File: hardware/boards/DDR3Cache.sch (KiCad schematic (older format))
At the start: 3 parts, among them U1 ECP5UM5G-381caBGA, U4 IS43TR16256B-125KBL

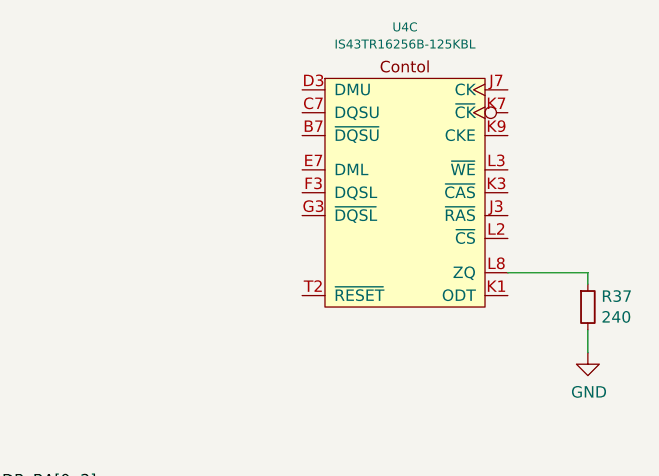
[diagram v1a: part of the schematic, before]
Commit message: Some ERC cleanup
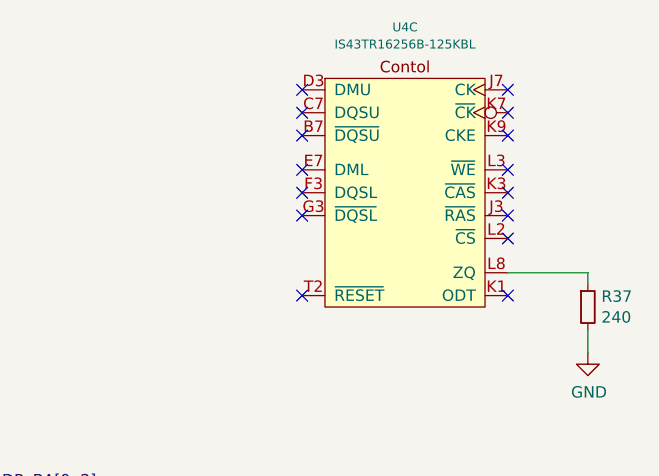
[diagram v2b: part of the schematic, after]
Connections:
- no-connect marks 65 -> 80
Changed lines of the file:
@@
 Wire Wire Line
 	13200 2350 12850 2350
+NoConn ~ 11950 1550
+NoConn ~ 11950 1650
+NoConn ~ 11950 1750
+NoConn ~ 11950 1900
+NoConn ~ 11950 2000
+NoConn ~ 11950 2100
+NoConn ~ 11950 2450
+NoConn ~ 12850 2450
+NoConn ~ 12850 2200
+NoConn ~ 12850 2100
+NoConn ~ 12850 2000
+NoConn ~ 12850 1900
+NoConn ~ 12850 1750
+NoConn ~ 12850 1650
+NoConn ~ 12850 1550
 Wire Bus Line
-	10550 3100 10550 3300
+	9250 4000 9250 4700
 Wire Bus Line
 	9250 3100 9250 3800
 Wire Bus Line
-	9250 4000 9250 4700
+	10550 3500 10550 5000
 Wire Bus Line
-	10550 3500 10550 5000
+	10550 3100 10550 3300
 $EndSCHEMATC

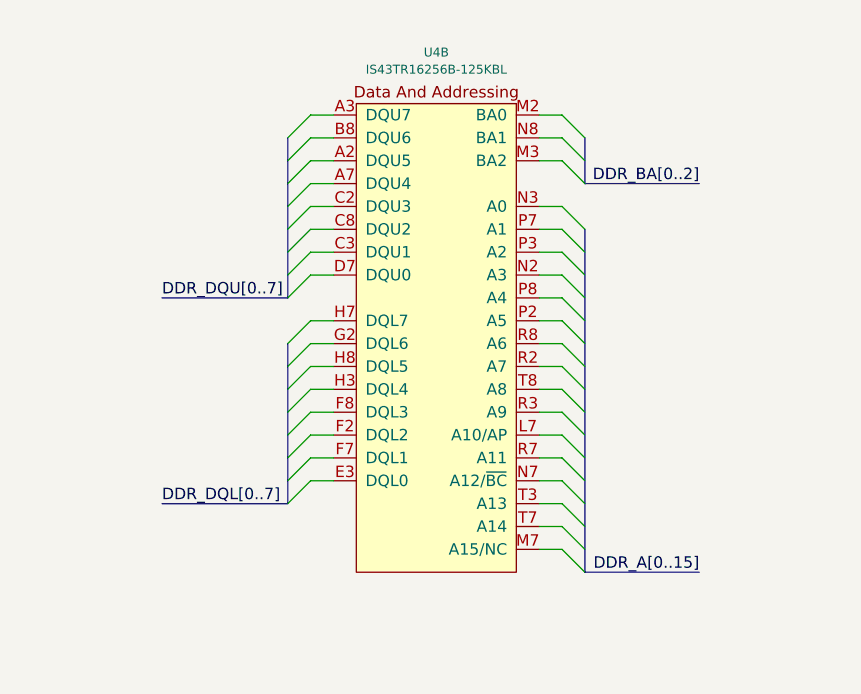
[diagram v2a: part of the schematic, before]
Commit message: Added headers for the SPI flash for both the FPGA and the PHY
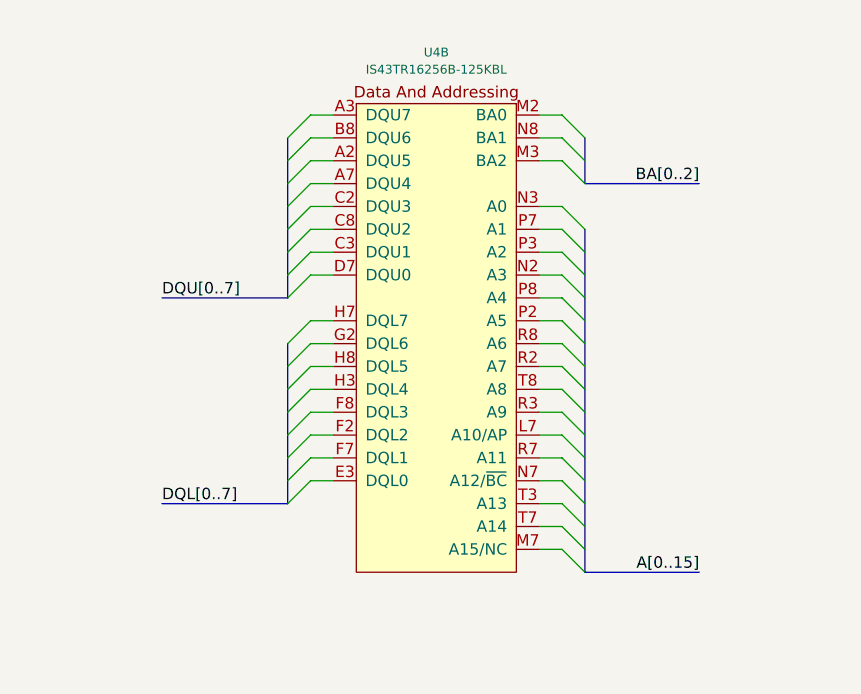
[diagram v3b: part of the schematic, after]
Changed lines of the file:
@@
 $Descr A3 16535 11693
 encoding utf-8
-Sheet 10 11
+Sheet 9 11
 Title "lethallink"
 Date "2020-06-13"
@@
 	9250 3800 8700 3800
 Text Label 11050 3300 2    50   ~ 0
-DDR_BA[0..2]
+BA[0..2]
 Text Label 11050 5000 2    50   ~ 0
-DDR_A[0..15]
+A[0..15]
 Text Label 8700 4700 0    50   ~ 0
-DDR_DQL[0..7]
+DQL[0..7]
 Text Label 8700 3800 0    50   ~ 0
-DDR_DQU[0..7]
+DQU[0..7]
 $Comp
 L Device:R_Small R37

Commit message: Some strugglebusting with the DDR interface
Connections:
- net BA2: now reaches U1.M3 (PL62B)
- net BA2: now also U4.M3 (BA2)
- net BA1: now reaches U1.N3 (PL62A)
- net BA1: now also U4.N8 (BA1)
- net A0: now reaches U1.P3 (PL68C/LLC/GPLL0T_IN)
- net A0: now also U4.N3 (A0)
- net BA0: now reaches U1.P5 (PL59D)
- net BA0: now also U4.M2 (BA0)
- net A14: now reaches U1.A3 (PL14C)
- net A14: now also U4.T7 (A14)
- net A4: now reaches U1.B3 (PL14D)
- net A4: now also U1.D2 (PL26C), U4.P8 (A4)
- net A11: now reaches U1.B4 (PL14B)
- net A11: now also U4.R7 (A11)
- net A6: now reaches U1.B5 (PL11C)
- net A6: now also U4.R8 (A6)
- net A12: now reaches U1.C3 (PL17C)
- net A12: now also U4.N7 (A12/~BC)
- net A1: now reaches U1.C4 (PL14A)
- net A1: now also U4.P7 (A1)
- net A8: now reaches U1.C5 (PL11D)
- net A8: now also U4.T8 (A8)
- net A13: now reaches U1.D3 (PL17D)
- net A13: now also U4.T3 (A13)
- net A10: now reaches U1.D5 (PL17B)
- net A10: now also U4.L7 (A10/AP)
- net A9: now reaches U1.E3 (PL20B)
- net A9: now also U4.R3 (A9)
- net A7: now reaches U1.E4 (PL17A)
- net A7: now also U4.R2 (A7)
- net A2: now reaches U1.E5 (PL20C)
- net A2: now also U4.P3 (A2)
- net A5: now reaches U1.F4 (PL20A)
- net A5: now also U4.P2 (A5)
- net A3: now reaches U1.F5 (PL20D)
- net A3: now also U4.N2 (A3)
- net DQU5: now reaches U4.A2 (DQU5)
- net DQU7: now reaches U4.A3 (DQU7)
- net DQU4: now reaches U4.A7 (DQU4)
- net DQU6: now reaches U4.B8 (DQU6)
- net DQU3: now reaches U4.C2 (DQU3)
- net DQU1: now reaches U4.C3 (DQU1)
- net DQU2: now reaches U4.C8 (DQU2)
- net DQU0: now reaches U4.D7 (DQU0)
- net DQL0: now reaches U4.E3 (DQL0)
- net DQL2: now reaches U4.F2 (DQL2)
- net DQL1: now reaches U4.F7 (DQL1)
- net DQL3: now reaches U4.F8 (DQL3)
- net DQL6: now reaches U4.G2 (DQL6)
- net DQL4: now reaches U4.H3 (DQL4)
- net DQL7: now reaches U4.H7 (DQL7)
- net DQL5: now reaches U4.H8 (DQL5)
- net A15: now reaches U4.M7 (A15/NC)
- no-connect marks 80 -> 61

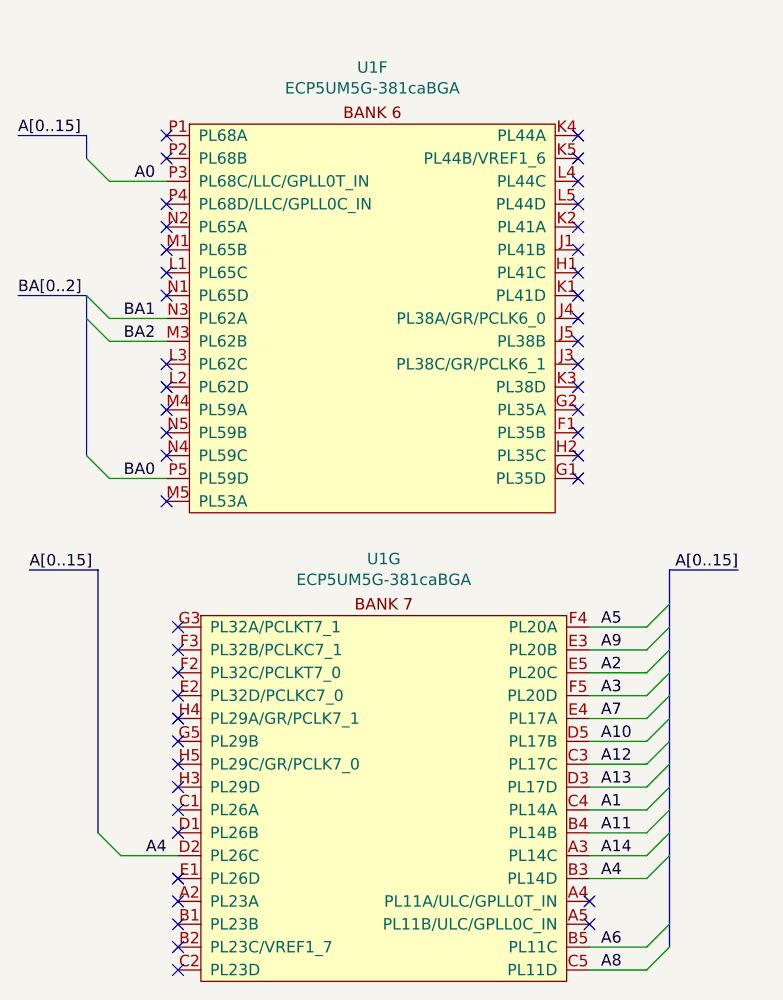
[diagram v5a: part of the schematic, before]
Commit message: Moved some things around swapping the DDR from banks 7 and 8 to banks 2 and 3, and moved the GPIFF 2 stuff to bank 7 to stop them from crossing over
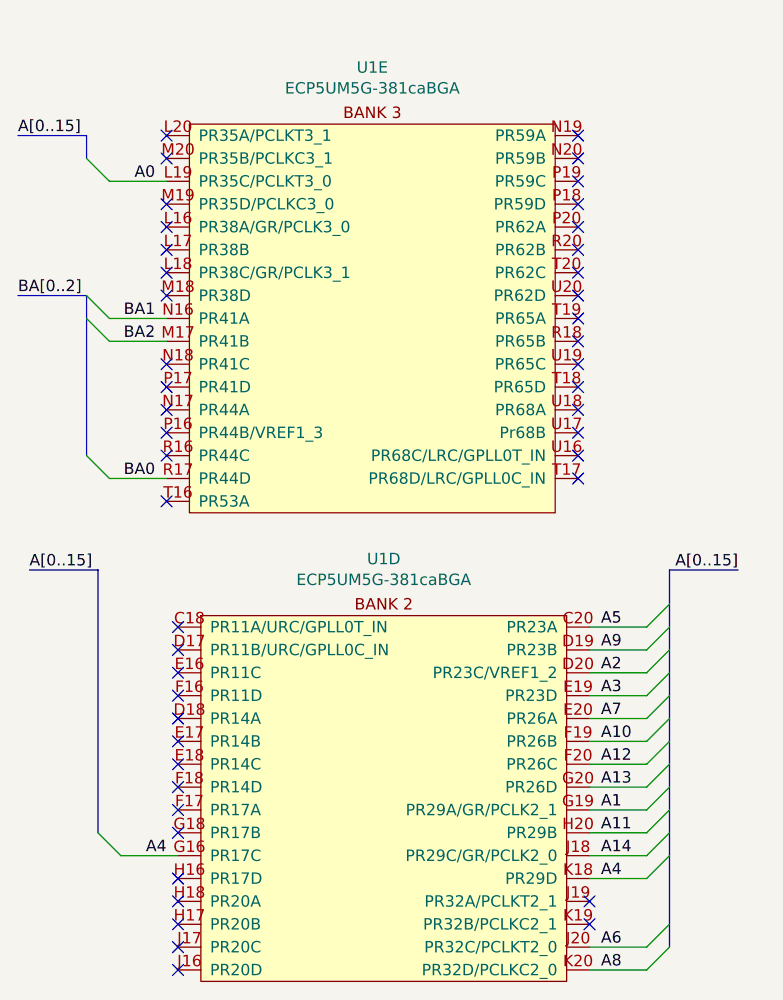
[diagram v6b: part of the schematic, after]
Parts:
- removed U1: ECP5UM5G-381caBGA, lethalbit:318caBGA, symbol lethalbit:ECP5UM5G-381caBGA
- added U1: ECP5UM5G-381caBGA, lethalbit:318caBGA, symbol lethalbit:ECP5UM5G-381caBGA
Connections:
- net A0: now also U1.L19 (PR35C/PCLKT3_0)
- net A1: now also U1.G19 (PR29A/GR/PCLK2_1)
- net A10: now also U1.F19 (PR26B)
- net A11: now also U1.H20 (PR29B)
- net A12: now also U1.F20 (PR26C)
- net A13: now also U1.G20 (PR26D)
- net A14: now also U1.J18 (PR29C/GR/PCLK2_0)
- net A2: now also U1.D20 (PR23C/VREF1_2)
- net A3: now also U1.E19 (PR23D)
- net A4: now also U1.G16 (PR17C), U1.K18 (PR29D)
- net A5: now also U1.C20 (PR23A)
- net A6: now also U1.J20 (PR32C/PCLKT2_0)
- net A7: now also U1.E20 (PR26A)
- net A8: now also U1.K20 (PR32D/PCLKC2_0)
- net A9: now also U1.D19 (PR23B)
- net BA0: now also U1.R17 (PR44D)
- net BA1: now also U1.N16 (PR41A)
- net BA2: now also U1.M17 (PR41B)
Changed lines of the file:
@@
 Comment4 ""
 $EndDescr
-$Comp
-L lethalbit:ECP5UM5G-381caBGA U1
-U 6 1 5F1BFFB3
-P 5850 1800
-F 0 "U1" H 5850 2148 50  0000 C CNN
-F 1 "ECP5UM5G-381caBGA" H 5850 2057 50  0000 C CNN
-F 2 "lethalbit:318caBGA" H 4500 1950 50  0001 C CNN
-F 3 "" H 4500 1950 50  0001 C CNN
-F 4 "Lattice" H 5850 1800 50  0001 C CNN "MFR"
-F 5 "LFE5UM5G-85F-8BG381I" H 5850 1800 50  0001 C CNN "MPN"
-F 6 "220-2112-ND" H 5850 1800 50  0001 C CNN "DIGIKEY_PN"
-	6    5850 1800
-	1    0    0    -1
-$EndComp
-$Comp
-L lethalbit:ECP5UM5G-381caBGA U1
-U 7 1 5F1BFFB9
-P 5900 3950
-F 0 "U1" H 5900 4298 50  0000 C CNN
-F 1 "ECP5UM5G-381caBGA" H 5900 4207 50  0000 C CNN
-F 2 "lethalbit:318caBGA" H 4550 4100 50  0001 C CNN
-F 3 "" H 4550 4100 50  0001 C CNN
-F 4 "Lattice" H 5900 3950 50  0001 C CNN "MFR"
-F 5 "LFE5UM5G-85F-8BG381I" H 5900 3950 50  0001 C CNN "MPN"
-F 6 "220-2112-ND" H 5900 3950 50  0001 C CNN "DIGIKEY_PN"
-	7    5900 3950
-	1    0    0    -1
-$EndComp
 NoConn ~ 4950 1750
 NoConn ~ 4950 1850
@@
 Wire Bus Line
 	4650 3650 4650 4800
+$Comp
+L lethalbit:ECP5UM5G-381caBGA U?
+U 4 1 5FCBABF4
+P 5900 3950
+AR Path="/5EF6A128/5FCBABF4" Ref="U?"  Part="4"
+AR Path="/5F2CAFD2/5FCBABF4" Ref="U?"  Part="4"
+AR Path="/5EDF3898/5FCBABF4" Ref="U1"  Part="4"
+F 0 "U1" H 5900 4298 50  0000 C CNN
+F 1 "ECP5UM5G-381caBGA" H 5900 4207 50  0000 C CNN
+F 2 "lethalbit:318caBGA" H 4550 4100 50  0001 C CNN
+F 3 "" H 4550 4100 50  0001 C CNN
+F 4 "Lattice" H 5900 3950 50  0001 C CNN "MFR"
+F 5 "LFE5UM5G-85F-8BG381I" H 5900 3950 50  0001 C CNN "MPN"
+F 6 "220-2112-ND" H 5900 3950 50  0001 C CNN "DIGIKEY_PN"
+	4    5900 3950
+	1    0    0    -1
+$EndComp
+$Comp
+L lethalbit:ECP5UM5G-381caBGA U?
+U 5 1 5FCF1F26
+P 5850 1800
+AR Path="/5EF67D90/5FCF1F26" Ref="U?"  Part="5"
+AR Path="/5F2CAFD2/5FCF1F26" Ref="U?"  Part="5"
+AR Path="/5EF6A128/5FCF1F26" Ref="U?"  Part="5"
+AR Path="/5EDF3898/5FCF1F26" Ref="U1"  Part="5"
+F 0 "U1" H 5850 2148 50  0000 C CNN
+F 1 "ECP5UM5G-381caBGA" H 5850 2057 50  0000 C CNN
+F 2 "lethalbit:318caBGA" H 4500 1950 50  0001 C CNN
+F 3 "" H 4500 1950 50  0001 C CNN
+F 4 "Lattice" H 5850 1800 50  0001 C CNN "MFR"
+F 5 "LFE5UM5G-85F-8BG381I" H 5850 1800 50  0001 C CNN "MPN"
+F 6 "220-2112-ND" H 5850 1800 50  0001 C CNN "DIGIKEY_PN"
+	5    5850 1800
+	1    0    0    -1
+$EndComp
+Wire Bus Line
+	4600 2450 4600 3150
 Wire Bus Line
 	10700 3100 10700 3300
 Wire Bus Line
-	4600 2450 4600 3150
-Wire Bus Line
 	9100 3100 9100 3800
